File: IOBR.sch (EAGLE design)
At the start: 10 parts, among them J1 Digital_0_7, J10 Power, J2 Analog, J3 Digital_8_13

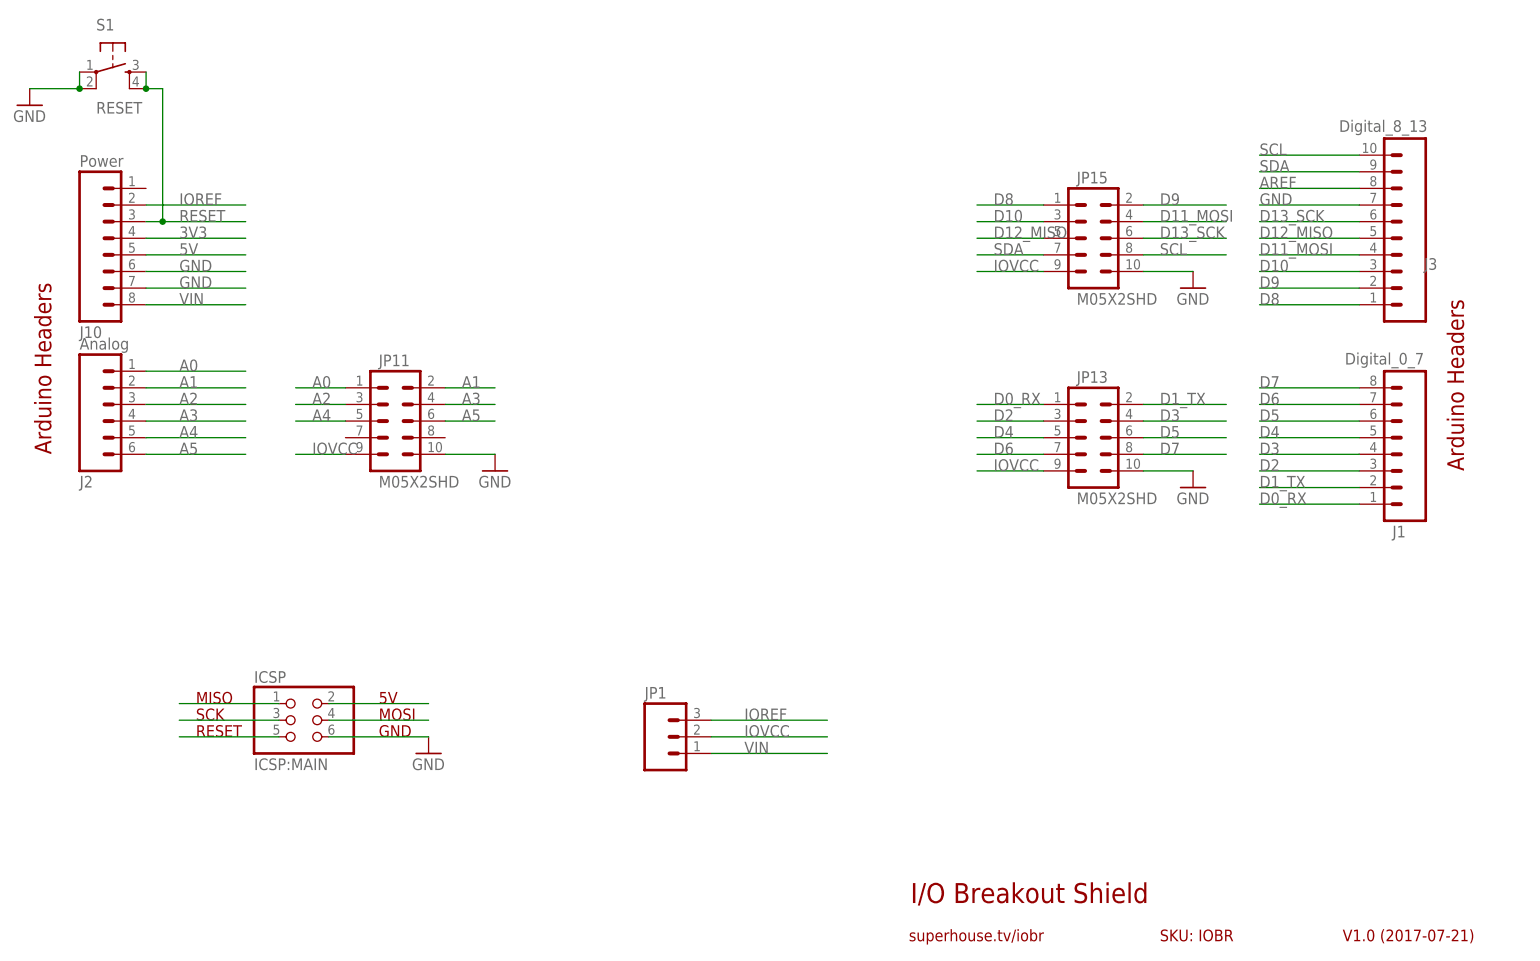
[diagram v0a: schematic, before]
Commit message: Expanded headers to 2x6 to include IOREF and RESET for v2.0 release
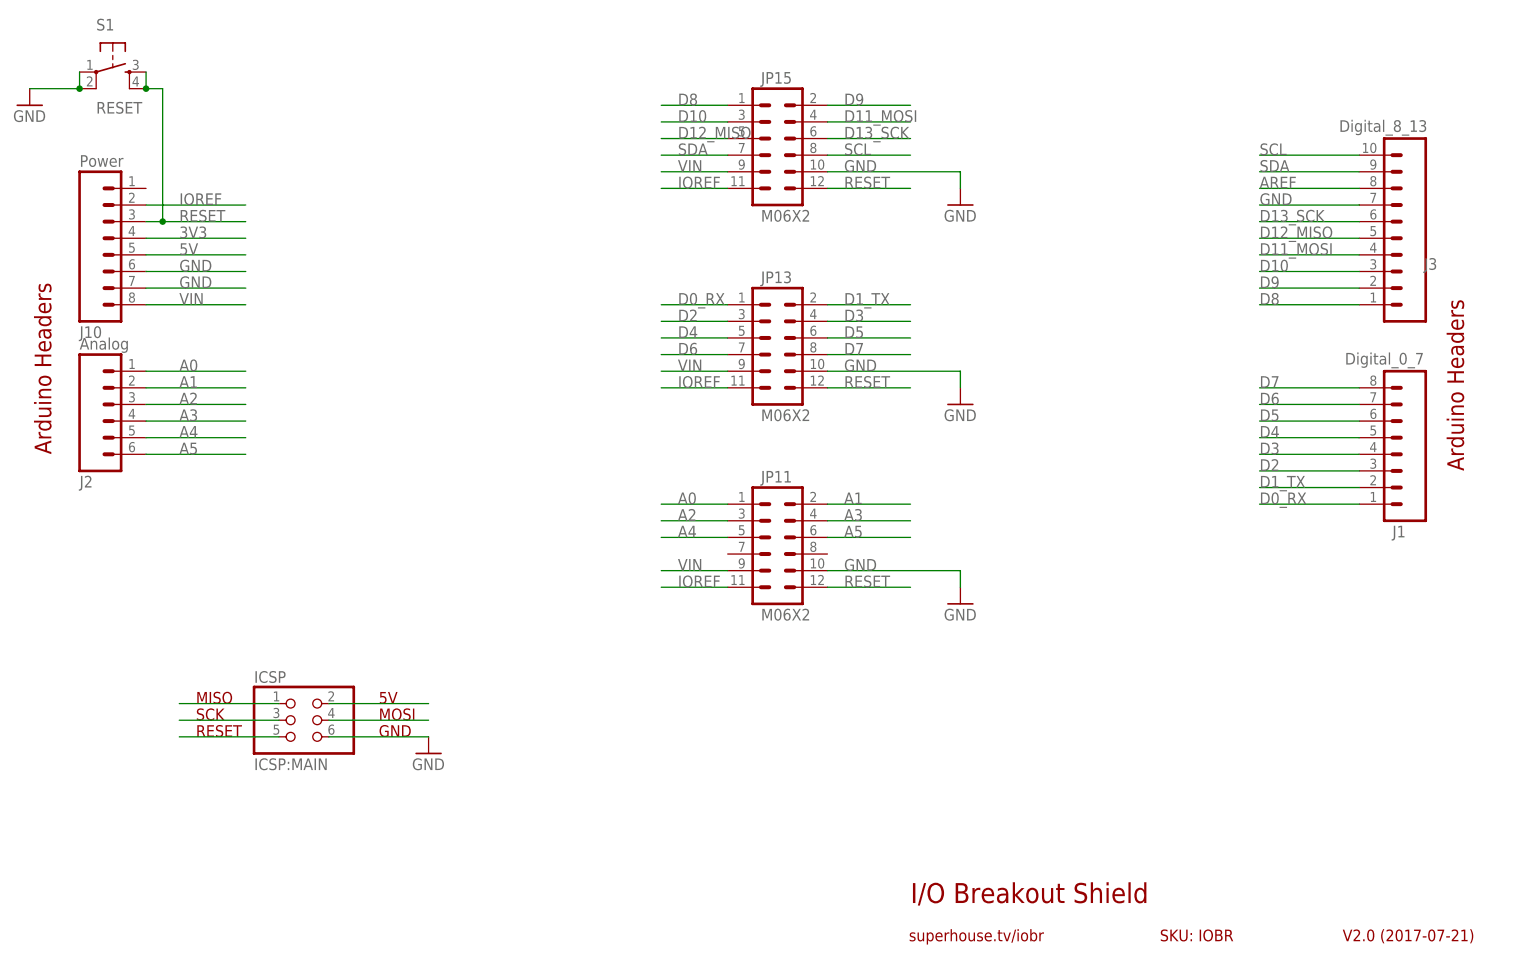
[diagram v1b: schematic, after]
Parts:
- removed JP1: (no value), freetronics-master-v1.1:M03PTH
- JP11, JP13, JP15: value M05X2SHD -> M06X2; device freetronics-original:M05X2SHD -> freetronics-jon:M06X2
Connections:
- removed net IOVCC: JP1.2, JP11.9, JP13.9, JP15.9
- net IOREF: now also JP11.11, JP13.11, JP15.11; no longer JP1.3
- net RESET: now also JP11.12, JP13.12, JP15.12
- net VIN: now also JP11.9, JP13.9, JP15.9; no longer JP1.1
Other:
- note added: "V2.0 (2017-07-21)"
- note removed: "V1.0 (2017-07-21)"

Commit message: Converted parts to SuperHouse libraries
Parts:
- ICSP: device pinhead:PINHD-2X3 -> SuperHouse-Connectors:ICSPPTH
- J1: device freetronics:M08 -> SuperHouse-Connectors:M08-PLAIN
- J10: device freetronics-master-v1:M08 -> SuperHouse-Connectors:M08-PLAIN
- J2: device freetronics-master-v1:M06SIP -> SuperHouse-Connectors:M06-PLAIN
- J3: device freetronics-original:M100.1 -> SuperHouse-Connectors:M10-PLAIN
- JP11, JP13, JP15: value M06X2 -> M06X2-SHROUDED; device freetronics-jon:M06X2 -> SuperHouse-Connectors:M06X2-SHROUDED
- S1: device freetronics-master-v1:TAC_SWITCHPTH -> SuperHouse-Switches:TAC_SWITCH-PTH-6

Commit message: Update for v2.1 release
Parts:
- removed ICSP: ICSP:MAIN, SuperHouse-Connectors:ICSPPTH
- removed J10: Power, SuperHouse-Connectors:M08-PLAIN
- removed JP11, JP13, JP15: M06X2-SHROUDED, SuperHouse-Connectors:M06X2-SHROUDED
- added J4: Power, SuperHouse-Connectors:M08-PIN-BELOW
- added J5: ICSP:MAIN, SuperHouse-Connectors:ICSP-ST-BELOW
- added J6, J7, J8: M02X6-SHROUDED, SuperHouse-Connectors:M02X6-SHROUDED
- J1: device SuperHouse-Connectors:M08-PLAIN -> SuperHouse-Connectors:M08-PIN-BELOW
- J2: device SuperHouse-Connectors:M06-PLAIN -> SuperHouse-Connectors:M06-PIN-BELOW
- J3: device SuperHouse-Connectors:M10-PLAIN -> SuperHouse-Connectors:M10-PIN-BELOW
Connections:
- net 3V3: now also J4.4; no longer J10.4
- net 5V: now also J4.5; no longer J10.5
- net A0: now also J8.1; no longer JP11.1
- net A1: now also J8.2; no longer JP11.2
- net A2: now also J8.3; no longer JP11.3
- net A3: now also J8.4; no longer JP11.4
- net A4: now also J8.5; no longer JP11.5
- net A5: now also J8.6; no longer JP11.6
- net D0_RX: now also J7.1; no longer JP13.1
- net D10: now also J6.3; no longer JP15.3
- net D11_MOSI: now also J6.4; no longer JP15.4
- net D12_MISO: now also J6.5; no longer JP15.5
- net D13_SCK: now also J6.6; no longer JP15.6
- net D1_TX: now also J7.2; no longer JP13.2
- net D2: now also J7.3; no longer JP13.3
- net D3: now also J7.4; no longer JP13.4
- net D4: now also J7.5; no longer JP13.5
- net D5: now also J7.6; no longer JP13.6
- net D6: now also J7.7; no longer JP13.7
- net D7: now also J7.8; no longer JP13.8
- net D8: now also J6.1; no longer JP15.1
- net D9: now also J6.2; no longer JP15.2
- net GND: now also J4.6, J4.7, J5.6, J6.10, J7.10, J8.10; no longer ICSP.6, J10.6, J10.7, JP11.10, JP13.10, JP15.10
- net IOREF: now also J4.2, J6.11, J7.11, J8.11; no longer J10.2, JP11.11, JP13.11, JP15.11
- net N$186: now also J5.1; no longer ICSP.1
- net N$187: now also J5.3; no longer ICSP.3
- net N$188: now also J5.5; no longer ICSP.5
- net N$197: now also J5.2; no longer ICSP.2
- net N$198: now also J5.4; no longer ICSP.4
- net RESET: now also J4.3, J6.12, J7.12, J8.12; no longer J10.3, JP11.12, JP13.12, JP15.12
- net SCL: now also J6.8; no longer JP15.8
- net SDA: now also J6.7; no longer JP15.7
- net VIN: now also J4.8, J6.9, J7.9, J8.9; no longer J10.8, JP11.9, JP13.9, JP15.9
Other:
- note added: "V2.1 (2019-10-25)"
- note removed: "V2.0 (2017-07-21)"
